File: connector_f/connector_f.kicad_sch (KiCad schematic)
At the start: 33 parts, among them J1 PowerOut, J2 PowerIn, J3 CANFD_In, U1 SKA2P1_TX, U2 TJA1042T, U3 SKA2P1_RX, U5 XC6206P182MR, U6 LSF0102DCUR

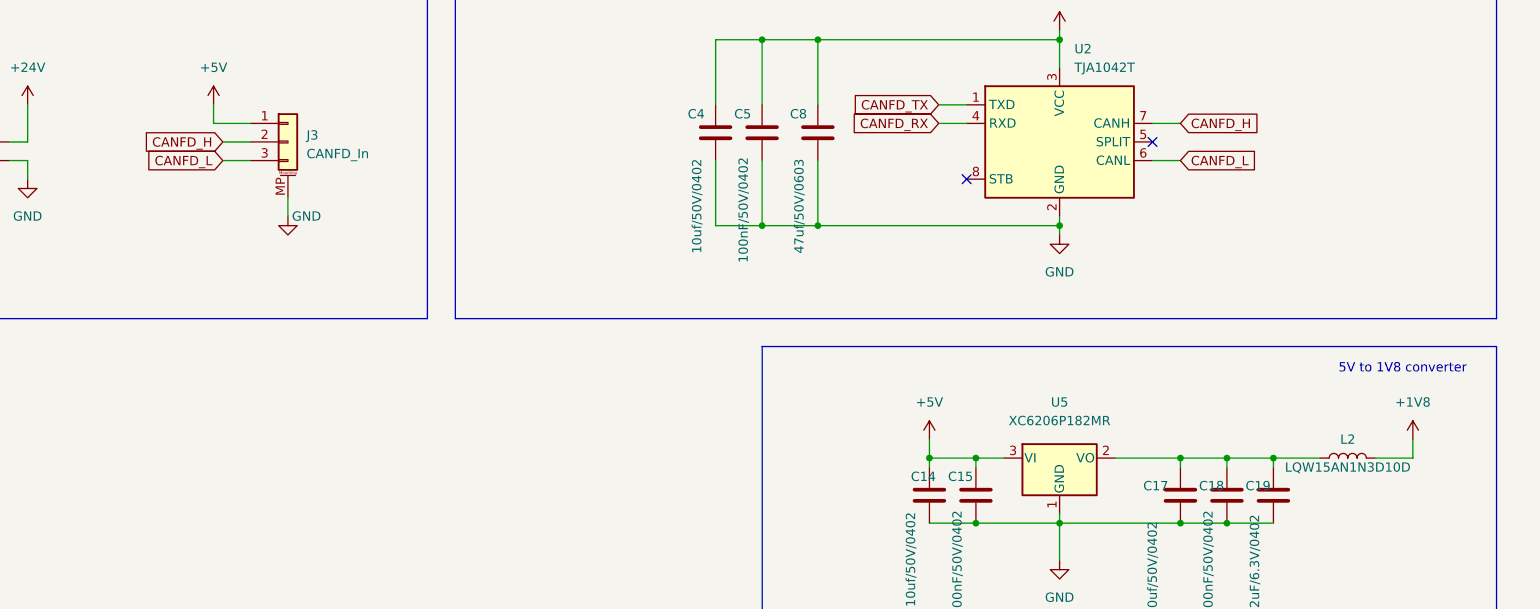
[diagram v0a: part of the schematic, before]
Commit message: [Fix] Manufacture modification
Signed-off-by: Homalozoa <nx.tardis@gmail.com>
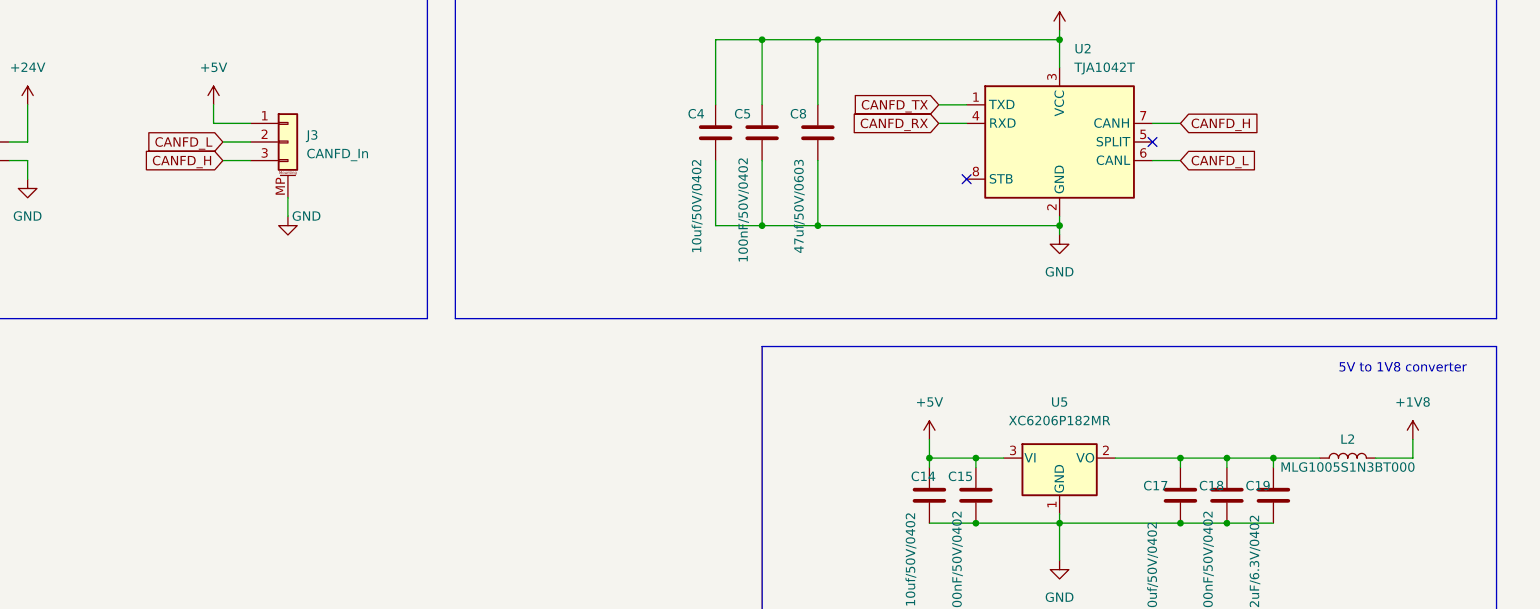
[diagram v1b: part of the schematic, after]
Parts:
- L2: value LQW15AN1N3D10D -> MLG1005S1N3BT000
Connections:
- net CANFD_H: now also J3.3 (Pin_3); no longer J3.2 (Pin_2)
- net CANFD_L: now also J3.2 (Pin_2); no longer J3.3 (Pin_3)
